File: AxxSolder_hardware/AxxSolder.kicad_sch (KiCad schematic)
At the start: 140 parts, among them IC1 OPA2387DSGT, IC2 TPD4E1B06DRLR, IC3 TPS54302DDCR, IC4 STUSB4500QTR, IC5 LTC4440AHMS8E, IC6 MAX16171ATA_VY+T, IC7 STM32G431CBT6, J1 USB4110-GF-A, J2 691243110009, J3 61300611821, J4 TSW-102-07-T-S, J5 TSW-102-07-T-S, Q1 STL9P3LLH6, Q2 2N7002NXAKR, Q3 STL10N3LLH5, U2 PEC11J-9215F-S0015, U4 BSC014N04LS

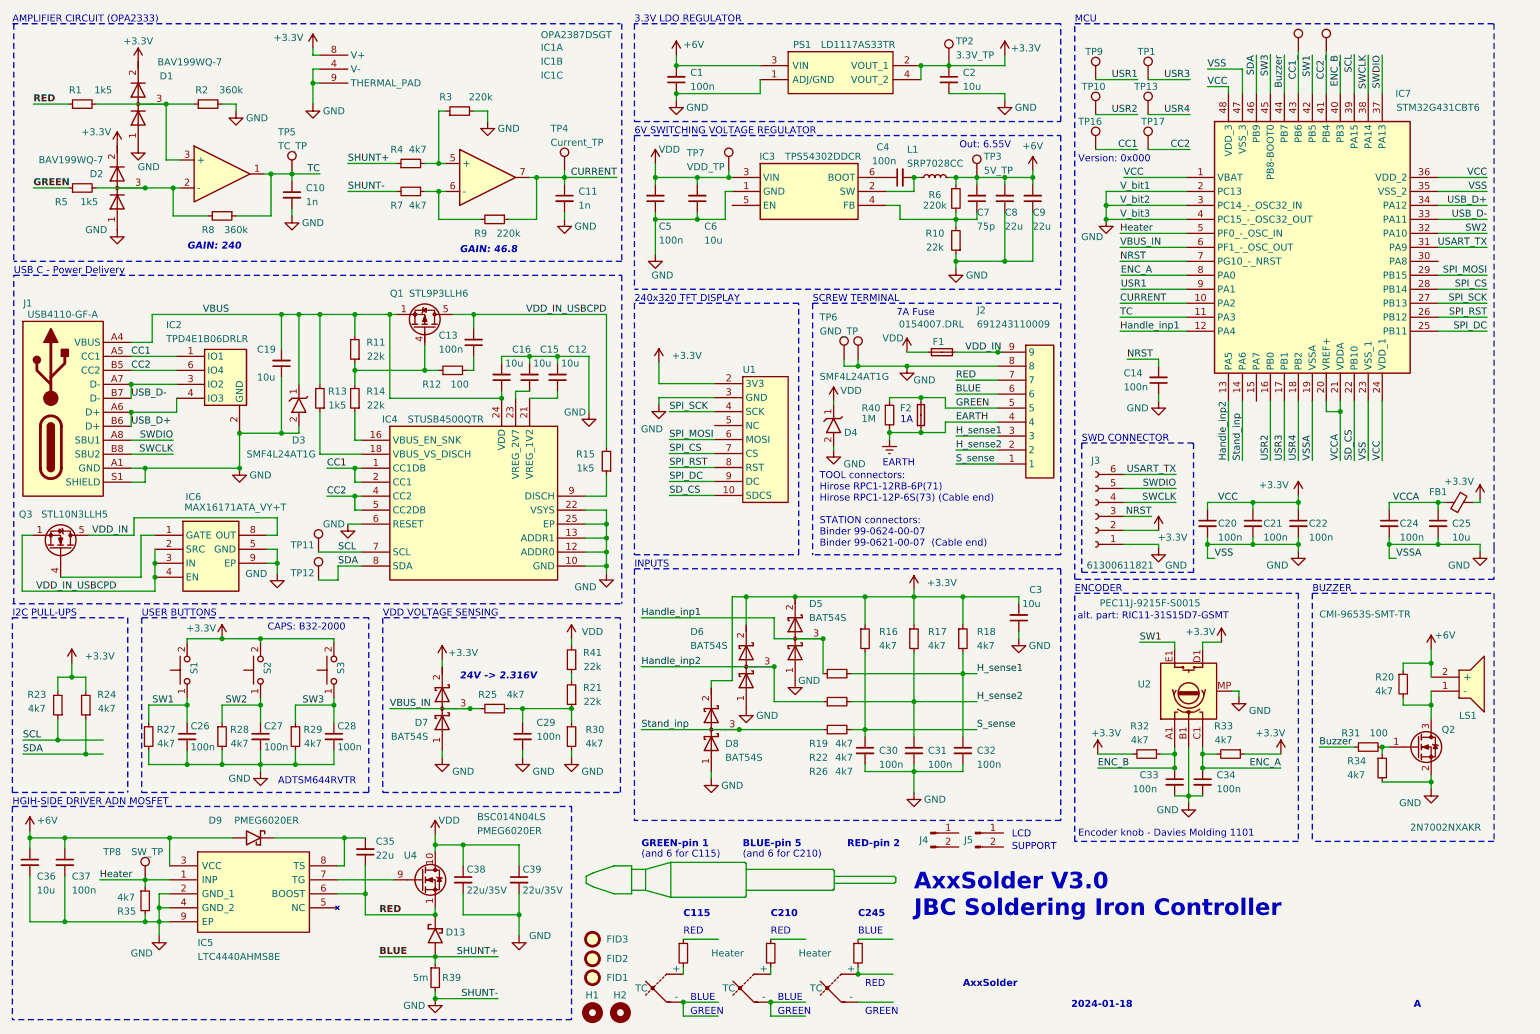
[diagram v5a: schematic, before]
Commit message: Updates on hardware, new DC-DC step down driver, new LDO, new ESD protection for USB, new Capacitor selection on input
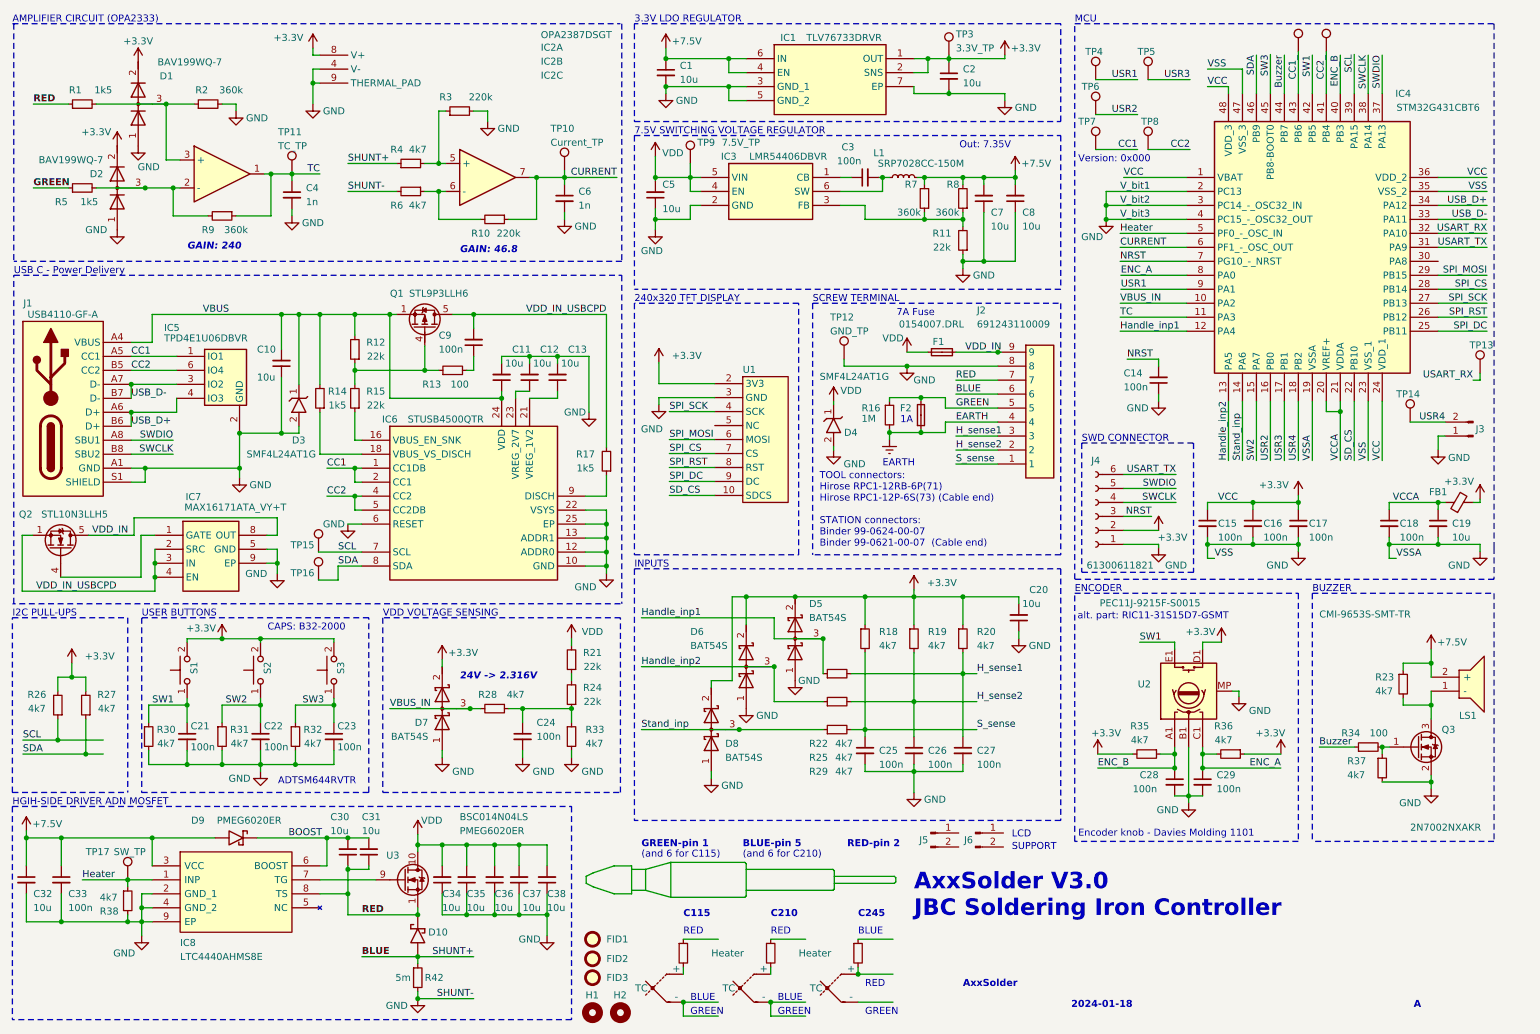
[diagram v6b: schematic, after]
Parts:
- removed C39: 22u/35V, Capacitor_SMD:C_1206_3216Metric, symbol Device:C_Small
- removed C5: 100n, Capacitor_SMD:C_0603_1608Metric, symbol Device:C_Small
- removed C9: 22u, Capacitor_SMD:C_1206_3216Metric, symbol Device:C_Small
- removed IC2: TPD4E1B06DRLR, footprints:SOTFL50P160X60-6N, symbol TPD4E1B06DRLR:TPD4E1B06DRLR
- removed IC3: TPS54302DDCR, footprints:SOT95P280X110-6N, symbol TPS54302DDCR:TPS54302DDCR
- removed L1: SRP7028CC, footprints:INDPM7366X300N, symbol SRP7028CC-100M:SRP7028CC-100M
- removed PS1: LD1117AS33TR, footprints:SOT230P700X190-4N, symbol LD1117AS33TR:LD1117AS33TR
- removed R6: 220k, Resistor_SMD:R_0603_1608Metric, symbol Device:R_Small
- removed TP3: 5V_TP, TestPoint:TestPoint_THTPad_D1.0mm_Drill0.5mm, symbol Connector:TestPoint
- removed TP6: GND_TP, TestPoint:TestPoint_THTPad_D2.0mm_Drill1.0mm, symbol Connector:TestPoint
- removed TP7: VDD_TP, TestPoint:TestPoint_THTPad_D1.0mm_Drill0.5mm, symbol Connector:TestPoint
- added C30, C31, C34, C36, C37: 10u, Capacitor_SMD:C_0603_1608Metric, symbol Device:C_Small
- added IC1: TLV76733DRVR, footprints:SON65P200X200X80-7N, symbol TLV76733DRVR:TLV76733DRVR
- added IC3: LMR54406DBVR, SOT95P280X145-6N, symbol LMR54406DBVR:LMR54406DBVR
- added IC5: TPD4E1U06DBVR, SOT95P280X145-6N, symbol TPD4E1U06DBVR:TPD4E1U06DBVR
- added J3: TSW-102-07-T-S, Connector_PinHeader_2.54mm:PinHeader_1x02_P2.54mm_Vertical, symbol TSW-102-07-T-S:TSW-102-07-T-S
- added L1: SRP7028CC-150M, footprints:INDPM7366X300N, symbol SRP7028CC-150M:SRP7028CC-150M
- added R7, R8: 360k, Resistor_SMD:R_0603_1608Metric, symbol Device:R_Small
- added TP13: DIAG_TP, Connector_PinSocket_2.54mm:PinSocket_1x01_P2.54mm_Vertical, symbol Connector:TestPoint
- added TP9: 7.5V_TP, TestPoint:TestPoint_Pad_D1.0mm, symbol Connector:TestPoint
- C1: value 100n -> 10u; Manufacturer_Name KEMET -> Murata Electronics; Manufacturer_Part_Number C0603C104J5RACTU -> GRM188R6YA106MA73J; Mouser Part Number 80-C0603C104J5R -> 81-GRM188R6YA106MA3J
- C35, C8: value 22u -> 10u; footprint Capacitor_SMD:C_1206_3216Metric -> Capacitor_SMD:C_0603_1608Metric; Manufacturer_Name Samsung Electro-Mechanics -> Murata Electronics; Manufacturer_Part_Number CL31A226MOCLNNC -> GRM188R6YA106MA73J; Mouser Part Number 187-CL31A226MOCLNNC -> 81-GRM188R6YA106MA3J
- C38: value 22u/35V -> 10u; footprint Capacitor_SMD:C_1206_3216Metric -> Capacitor_SMD:C_0603_1608Metric; Manufacturer_Name TDK -> Murata Electronics; Manufacturer_Part_Number C3216X5R1V226M160AC -> GRM188R6YA106MA73J; Mouser Part Number 810-C3216X5R1V226M -> 81-GRM188R6YA106MA3J
- C7: value 75p -> 10u; Manufacturer_Name KEMET -> Murata Electronics; Manufacturer_Part_Number C0603C750K5HACTU -> GRM188R6YA106MA73J; Mouser Part Number 80-C0603C750K5HACTU -> 81-GRM188R6YA106MA3J
- Q2: renamed from Q3; footprint STL10N3LLH5 -> footprints:STL10N3LLH5
- TP12: renamed from TP14; value TC_TP -> GND_TP
- TP3: renamed from TP2; footprint TestPoint:TestPoint_THTPad_D1.0mm_Drill0.5mm -> TestPoint:TestPoint_Pad_D1.0mm
- renumbered C19 to C10, C16 to C11, C15 to C12, C12 to C13, C20 to C15, C21 to C16, C22 to C17, C24 to C18, C25 to C19, C3 to C20, C26 to C21, C27 to C22, C28 to C23, C29 to C24, C30 to C25, C31 to C26, C32 to C27, C33 to C28, C34 to C29, C4 to C3, C36 to C32, C37 to C33, C10 to C4, C6 to C5, C11 to C6, C13 to C9, D13 to D10, FID3 to FID1, FID1 to FID3, IC1 to IC2, IC7 to IC4, IC4 to IC6, IC6 to IC7, IC5 to IC8, J3 to J4, J4 to J5, J5 to J6, Q2 to Q3, R9 to R10, R10 to R11, R11 to R12, R12 to R13, R13 to R14, R14 to R15, R40 to R16, R15 to R17, R16 to R18, R17 to R19, R18 to R20, R41 to R21, R19 to R22, R20 to R23, R21 to R24, R22 to R25, R23 to R26, R24 to R27, R25 to R28, R26 to R29, R27 to R30, R28 to R31, R29 to R32, R30 to R33, R31 to R34, R32 to R35, R33 to R36, R34 to R37, R35 to R38, R36 to R39, R37 to R40, R38 to R41, R39 to R42, R7 to R6, R8 to R9, TP18 to TP1, TP4 to TP10, TP5 to TP11, TP13 to TP14, TP11 to TP15, TP12 to TP16, TP8 to TP17, TP19 to TP2, TP9 to TP4, TP1 to TP5, TP10 to TP6, TP16 to TP7, TP17 to TP8, U4 to U3
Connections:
- net +3.3V: now also IC1.1 (OUT), IC1.2 (SNS)
- net CC1: now also IC5.1 (IO1)
- net CC2: now also IC5.6 (IO4)
- net CURRENT: now also IC4.6 (PF1_-_OSC_OUT); no longer IC4.10 (PA2)
- net GND: now also C1.2, C35.1, C38.1, C7.1, C34.1, C36.1, C37.1, IC1.3 (GND_1), IC1.5 (GND_2), IC1.7 (EP), IC3.2 (GND), IC5.2 (GND), J3.1 (Pin_1); no longer C1.1, C38.2
- net RED: now also IC8.8 (TS), C30.1, C31.1; no longer C35.1, IC8.6 (BOOST)
- net SW2: now also IC4.15 (PA7); no longer IC4.32 (PA10)
- net USB_D+: now also IC5.4 (IO3)
- net USB_D-: now also IC5.3 (IO2)
- net USR4: now also J3.2 (Pin_2)
- net VBUS_IN: now also IC4.10 (PA2); no longer IC4.6 (PF1_-_OSC_OUT)
- net VDD: now also C35.2, C38.2, C34.2, C36.2, C37.2, IC3.4 (EN), IC3.5 (VIN), TP9.1; no longer C38.1
- net at R11.2: now also IC3.3 (FB), R7.1, R8.1; no longer C7.1
- net at C3.2: now also IC3.6 (SW), L1.1
- net at C3.1: now also IC3.1 (CB)
- net +6V renamed +7.5V
- net +7.5V: now also C1.1, IC1.4 (EN), IC1.6 (IN), L1.2, R7.2, R8.2; no longer C1.2
- new net BOOST: C30.2, C31.2, D9.1, IC8.6 (BOOST)
- new net USART_RX: IC4.32 (PA10), TP13.1
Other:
- note added: "7.5V SWITCHING VOLTAGE REGULATOR"
- note added: "Out: 7.35V"
- note removed: "6V SWITCHING VOLTAGE REGULATOR"
- note removed: "Out: 6.55V"
- moved on the sheet: C2, C3, C32, C33, C5, D10, D9, IC8, R11, R38, R42, TP14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

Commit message: update design with new electrolytic capacitor
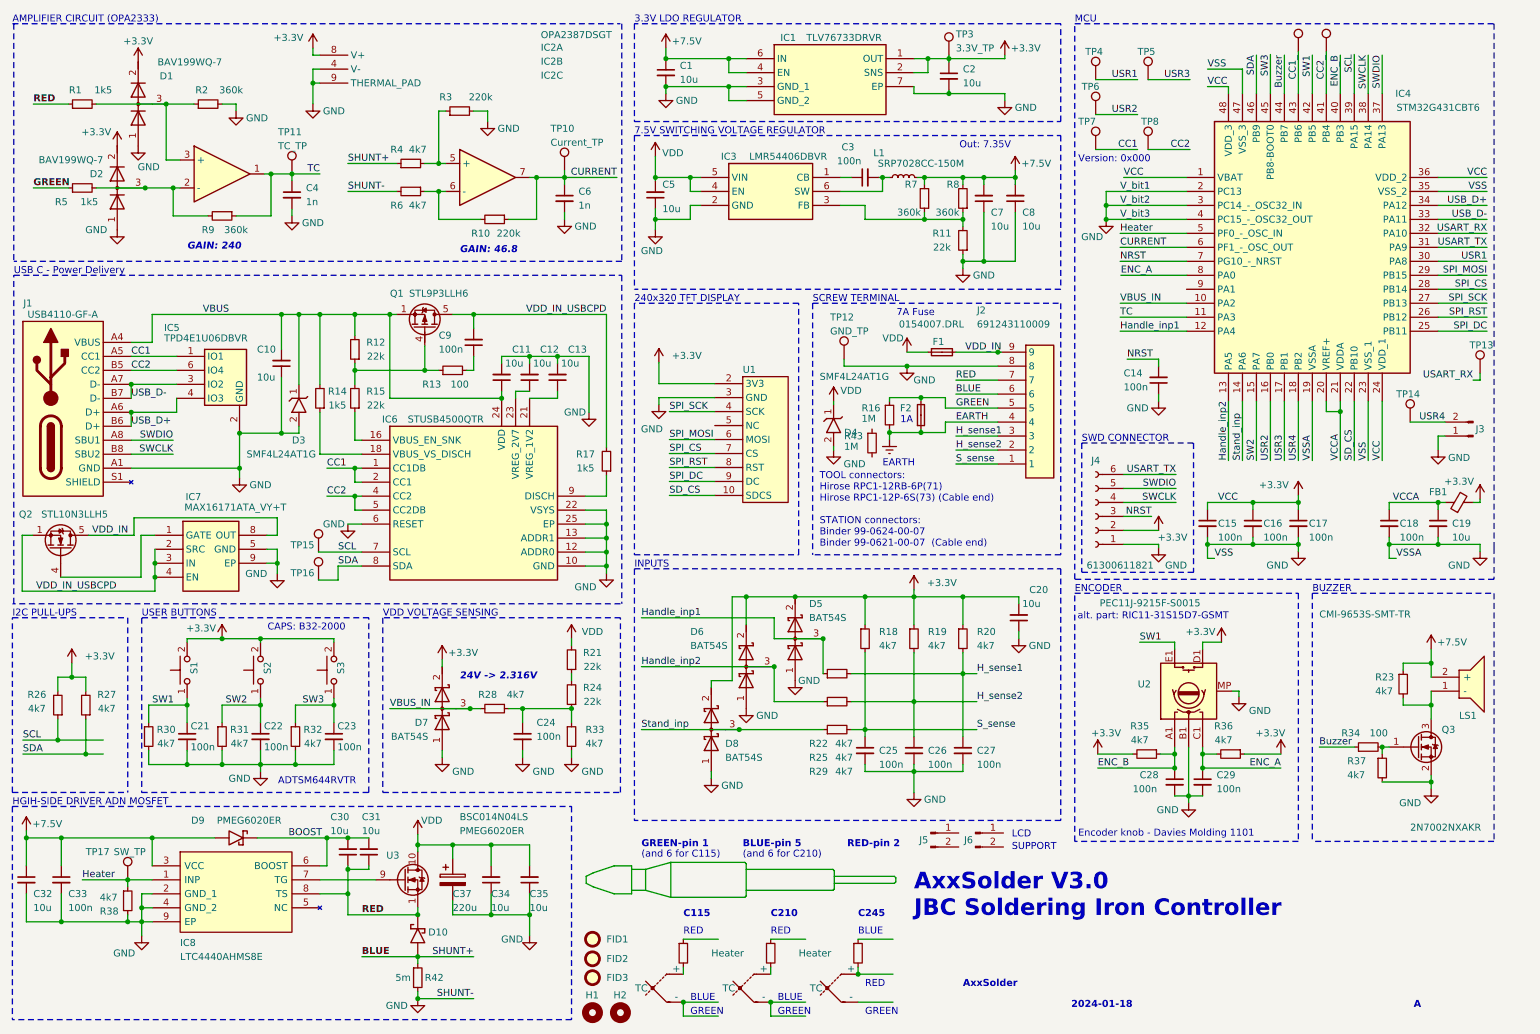
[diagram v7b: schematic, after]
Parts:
- removed C36, C37, C38: 10u, Capacitor_SMD:C_0603_1608Metric, symbol Device:C_Small
- removed TP9: 7.5V_TP, TestPoint:TestPoint_Pad_D1.0mm, symbol Connector:TestPoint
- added C37: 220u, CAPAE830X1050N, symbol EEV227M035A9MAA:EEV227M035A9MAA
- added R43: 1M, Resistor_SMD:R_1206_3216Metric, symbol Device:R_Small
- J1: footprint footprints:USB4110GFA -> USB4110GFA
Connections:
- net GND: now also C37.2; no longer J1.S1 (SHIELD)
- net USR1: now also IC4.30 (PA8); no longer IC4.9 (PA1)
- net VDD: now also C37.1
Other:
- moved on the sheet: C34, C35
